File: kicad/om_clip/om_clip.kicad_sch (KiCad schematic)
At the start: 18 parts, among them Q1 NPN, Q2 NPN, U1 LM393

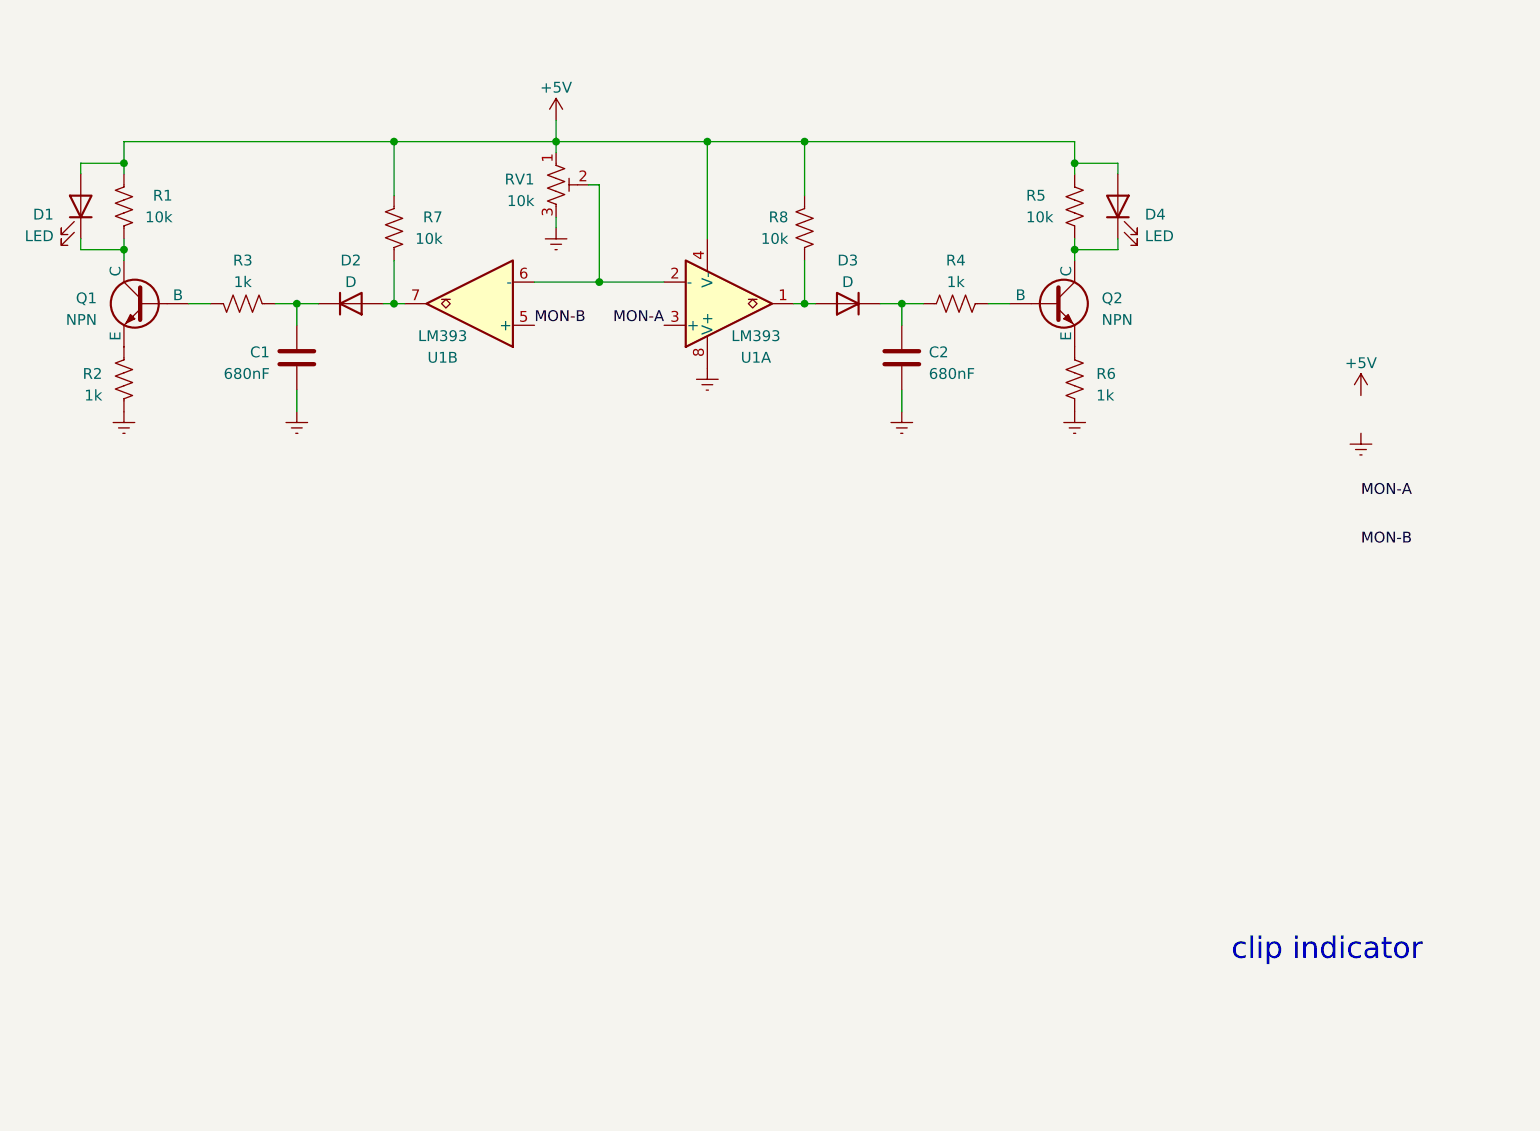
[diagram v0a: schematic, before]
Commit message: clip circuit improvements
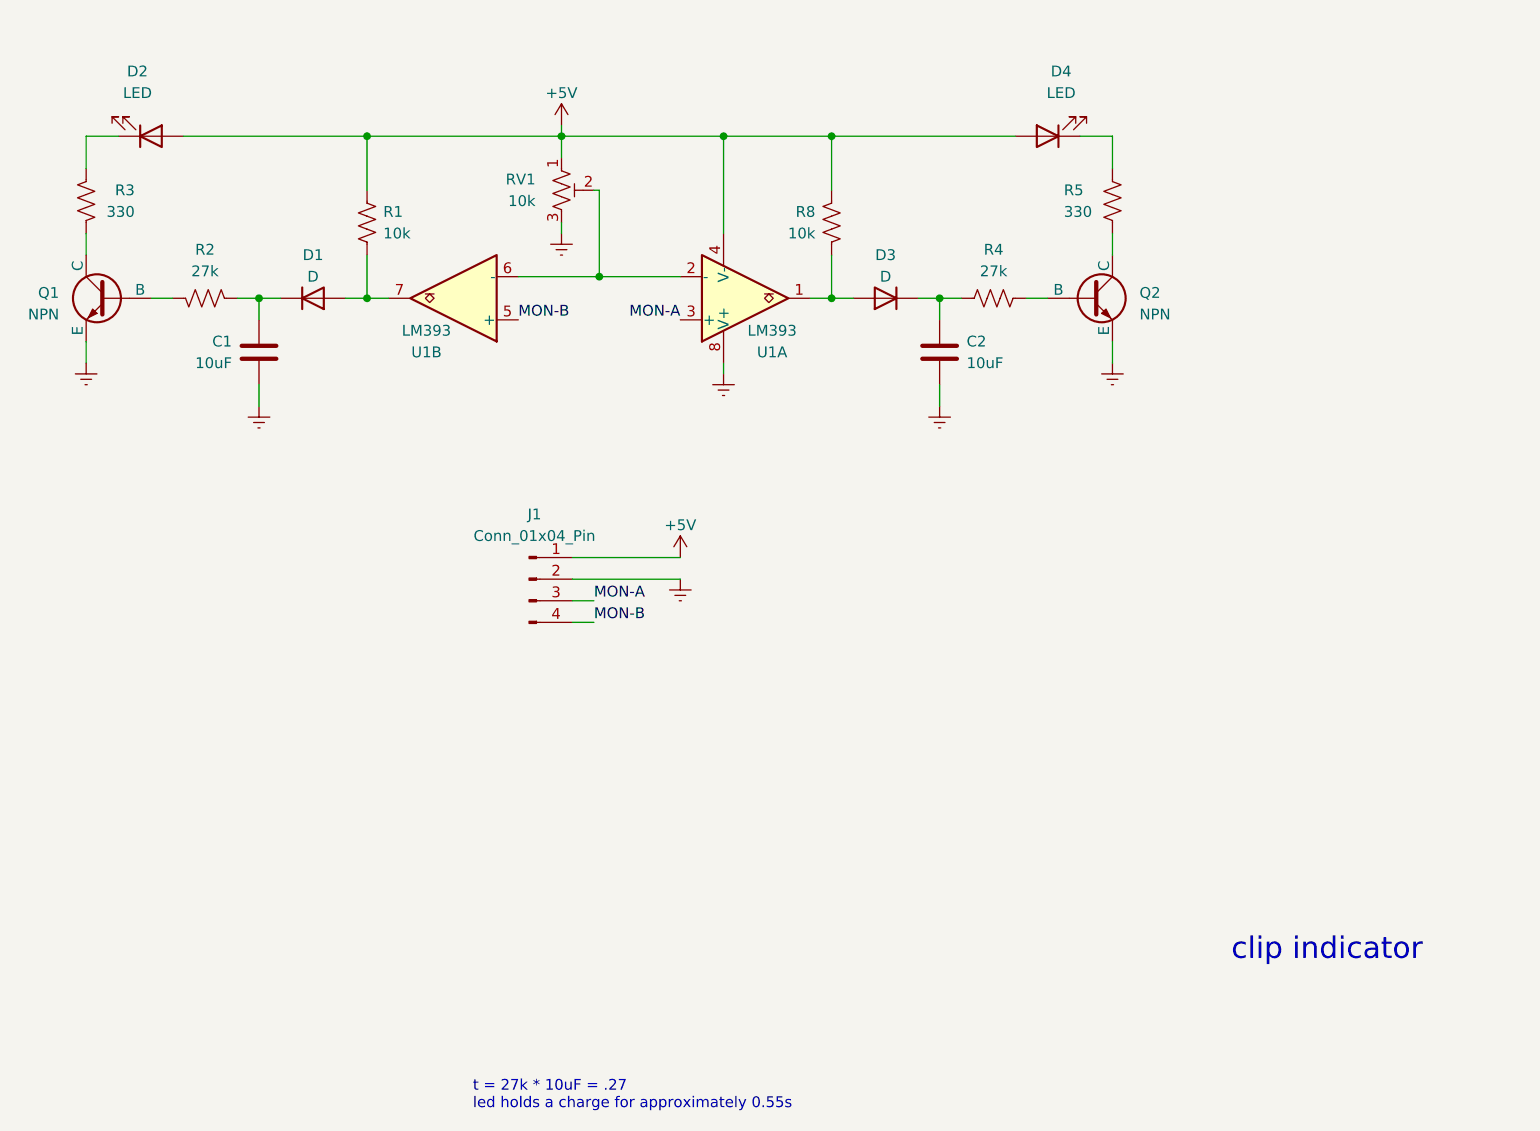
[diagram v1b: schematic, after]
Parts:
- removed D1: LED, symbol Device:LED
- removed D2: D, symbol Device:D
- removed R6: 1k, symbol Device:R_US
- removed R7: 10k, symbol Device:R_US
- added D1: D, symbol Device:D
- added D2: LED, symbol Device:LED
- added J1: Conn_01x04_Pin, symbol Connector:Conn_01x04_Pin
- C1, C2: value 680nF -> 10uF
- R2, R4: value 1k -> 27k
- R3: value 1k -> 330
- R5: value 10k -> 330
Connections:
- net +5V: now also D2.2 (A), J1.1 (Pin_1); no longer R5.2
- net Earth: now also Q1.3 (E), Q2.3 (E), J1.2 (Pin_2); no longer R2.1
- net MON-A: now also J1.3 (Pin_3)
- net MON-B: now also J1.4 (Pin_4)
- net at R3.1: now also Q1.1 (C); no longer C1.1
- net at U1.7: now also R1.1, D1.2 (A)
- net at R3.2: now also D2.1 (K); no longer Q1.2 (B)
- net at R2.2: now also Q1.2 (B); no longer Q1.3 (E)
- net at Q2.1 (C), R5.1: no longer D4.1 (K)
- new net: C1.1, D1.1 (K), R2.1
- new net: D4.1 (K), R5.2
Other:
- note added: "t = 27k * 10uF = .27 led holds a charge for approximately 0.55s"
- moved on the sheet: C2, D3, D4, Q2, R4, R5, R8, RV1, U1A, U1B

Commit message: changed to 9v rails
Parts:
- removed J1: Conn_01x04_Pin, symbol Connector:Conn_01x04_Pin
- added J2: Conn_01x06_Pin, symbol Connector:Conn_01x06_Pin
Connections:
- net +5V: now also J2.1 (Pin_1); no longer R1.2, R8.2, RV1.1, U1.4 (V-)
- net Earth: now also J2.4 (Pin_4); no longer C1.2, C2.2, U1.8 (V+)
- net MON-A: now also J2.5 (Pin_5)
- net MON-B: now also J2.6 (Pin_6)
- new net +9V: J2.2 (Pin_2), R1.2, R8.2, RV1.1, U1.4 (V-)
- new net -9V: C1.2, C2.2, J2.3 (Pin_3), U1.8 (V+)
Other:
- moved on the sheet: D2, D4

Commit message: 15v rails
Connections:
- net -9V: no longer C1.2, C2.2, J2.3 (Pin_3)
- net +9V renamed +15V
- new net -15V: C1.2, C2.2, J2.3 (Pin_3)

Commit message: 15v rails
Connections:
- net -9V is gone; now on net -15V: U1.8 (V+)
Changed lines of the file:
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@@
-	)
-	(symbol
-		(lib_id "power:-9V")
-		(at 158.75 105.41 180)
-		(unit 1)
-		(exclude_from_sim no)
-		(in_bom yes)
-		(on_board yes)
-		(dnp no)
-		(fields_autoplaced yes)
-		(property "Reference" "#PWR012"
-			(at 158.75 101.6 0)
-			(effects
-				(font
-					(size 1.27 1.27)
-				)
-				(hide yes)
-			)
-		)
-		(property "Value" "-9V"
-			(at 158.75 110.49 0)
-			(effects
-				(font
-					(size 1.27 1.27)
-				)
-			)
-		)
-		(property "Footprint" ""
-			(at 158.75 105.41 0)
-			(effects
-				(font
-					(size 1.27 1.27)
-				)
-				(hide yes)
-			)
-		)
-		(property "Datasheet" ""
-			(at 158.75 105.41 0)
-			(effects
-				(font
-					(size 1.27 1.27)
-				)
-				(hide yes)
-			)
-		)
-		(property "Description" "Power symbol creates a global label with name \"-9V\""
-			(at 158.75 105.41 0)
-			(effects
-				(font
-					(size 1.27 1.27)
-				)
-				(hide yes)
-			)
-		)
-		(pin "1"
-		)
-		(instances
-			(project "om_clip"
-				(path "/1547e3d7-ae65-43bd-9639-7774ac63921b"
-					(reference "#PWR012")
-					(unit 1)
-				)
-			)
-		)
 	)
 	(symbol
@@
 					(unit 1)
 				)
+			)
+		)
+	)
+	(symbol
+		(lib_id "power:-15V")
+		(at 158.75 105.41 180)
+		(unit 1)
+		(exclude_from_sim no)
+		(in_bom yes)
+		(on_board yes)
+		(dnp no)
+		(property "Reference" "#PWR06"
+			(at 158.75 101.6 0)
+			(effects
+				(font
+					(size 1.27 1.27)
+				)
+				(hide yes)
+			)
+		)
+		(property "Value" "-15V"
+			(at 159.004 109.728 0)
+			(effects
+				(font
+					(size 1.27 1.27)
+				)
+			)
+		)
+		(property "Footprint" ""
+			(at 158.75 105.41 0)
+			(effects
+				(font
+					(size 1.27 1.27)
+				)
+				(hide yes)
+			)
+		)
+		(property "Datasheet" ""
+			(at 158.75 105.41 0)
+			(effects
+				(font
+					(size 1.27 1.27)
+				)
+				(hide yes)
+			)
+		)
+		(property "Description" "Power symbol creates a global label with name \"-15V\""
+			(at 158.75 105.41 0)
+			(effects
+				(font
+					(size 1.27 1.27)
+				)
+				(hide yes)
+			)
+		)
+		(pin "1"
+		)
+		(instances
+			(project "om_clip"
+				(path "/1547e3d7-ae65-43bd-9639-7774ac63921b"
+					(reference "#PWR06")
+					(unit 1)
+				)

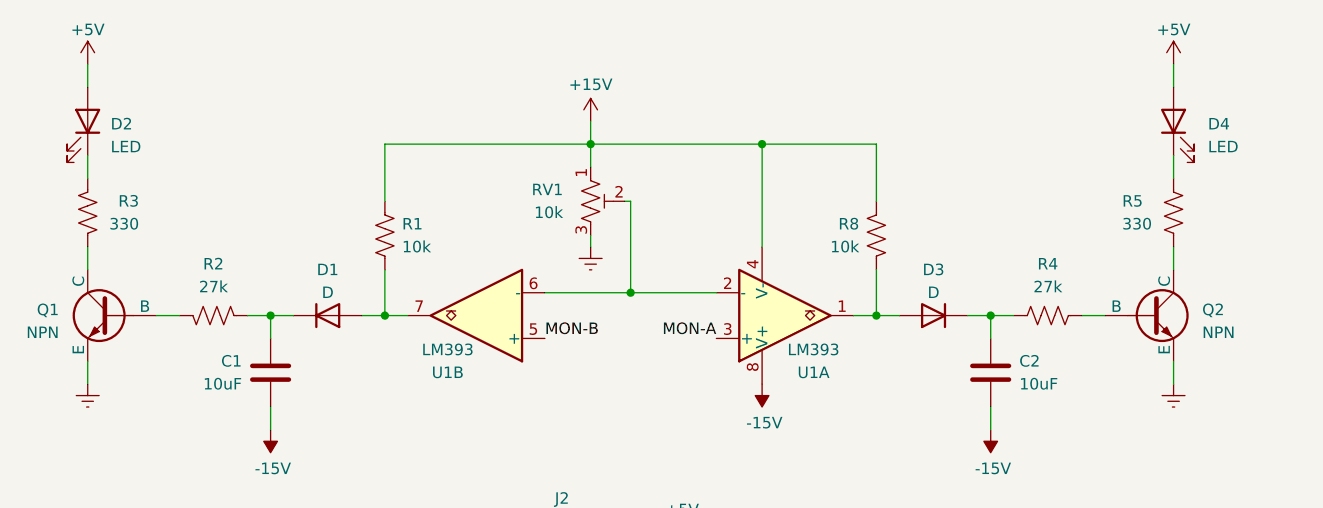
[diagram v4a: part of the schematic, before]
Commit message: 1k led resistors
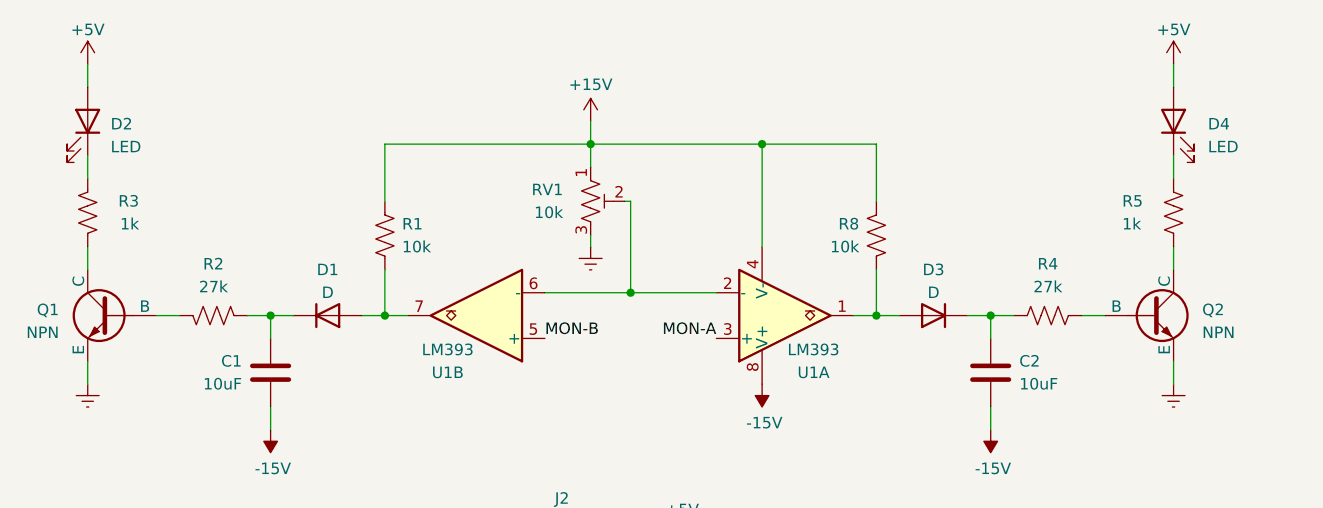
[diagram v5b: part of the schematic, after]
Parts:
- R3, R5: value 330 -> 1k
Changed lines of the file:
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@@
 			)
 		)
-		(property "Value" "330"
+		(property "Value" "1k"
 			(at 198.755 87.63 0)
 			(effects
@@
 			)
 		)
-		(property "Value" "330"
+		(property "Value" "1k"
 			(at 89.535 87.63 0)
 			(effects
